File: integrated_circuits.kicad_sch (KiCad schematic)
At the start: 14 parts

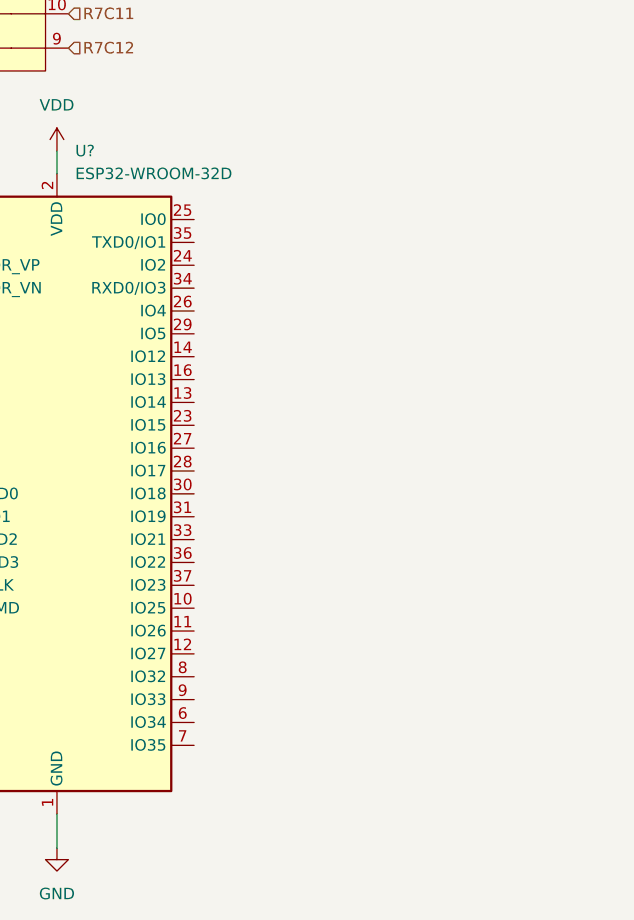
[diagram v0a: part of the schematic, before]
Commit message: Add MCU connections.
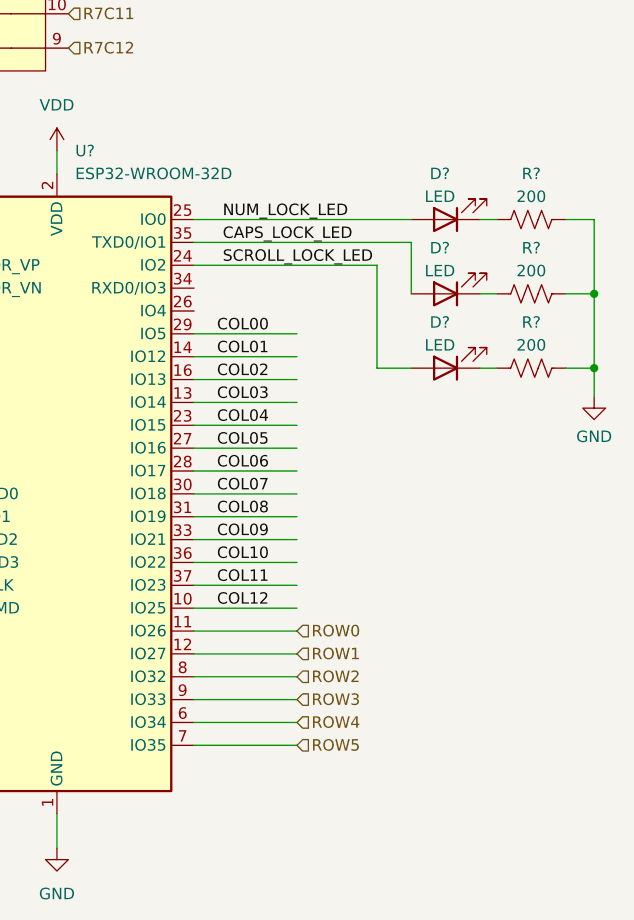
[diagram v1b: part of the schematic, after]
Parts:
- added D? (x3): LED, symbol Device:LED
- added R? (x3): 200, symbol Device:R_US
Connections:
- net GND: now also R?.2, R?.2, R?.2
- net COL12: now reaches U?.10 (IO25)
- net ROW0: now reaches U?.11 (IO26)
- net ROW1: now reaches U?.12 (IO27)
- net COL03: now reaches U?.13 (IO14)
- net COL01: now reaches U?.14 (IO12)
- net COL02: now reaches U?.16 (IO13)
- net COL04: now reaches U?.23 (IO15)
- net SCROLL_LOCK_LED: now reaches U?.24 (IO2)
- net SCROLL_LOCK_LED: now also D?.2 (A)
- net NUM_LOCK_LED: now reaches U?.25 (IO0)
- net NUM_LOCK_LED: now also D?.2 (A)
- net COL05: now reaches U?.27 (IO16)
- net COL06: now reaches U?.28 (IO17)
- net COL00: now reaches U?.29 (IO5)
- net COL07: now reaches U?.30 (IO18)
- net COL08: now reaches U?.31 (IO19)
- net COL09: now reaches U?.33 (IO21)
- net CAPS_LOCK_LED: now reaches U?.35 (TXD0/IO1)
- net CAPS_LOCK_LED: now also D?.2 (A)
- net COL10: now reaches U?.36 (IO22)
- net COL11: now reaches U?.37 (IO23)
- net ROW4: now reaches U?.6 (IO34)
- net ROW5: now reaches U?.7 (IO35)
- net ROW2: now reaches U?.8 (IO32)
- net ROW3: now reaches U?.9 (IO33)
- new net: D?.1 (K), R?.1 (x3)

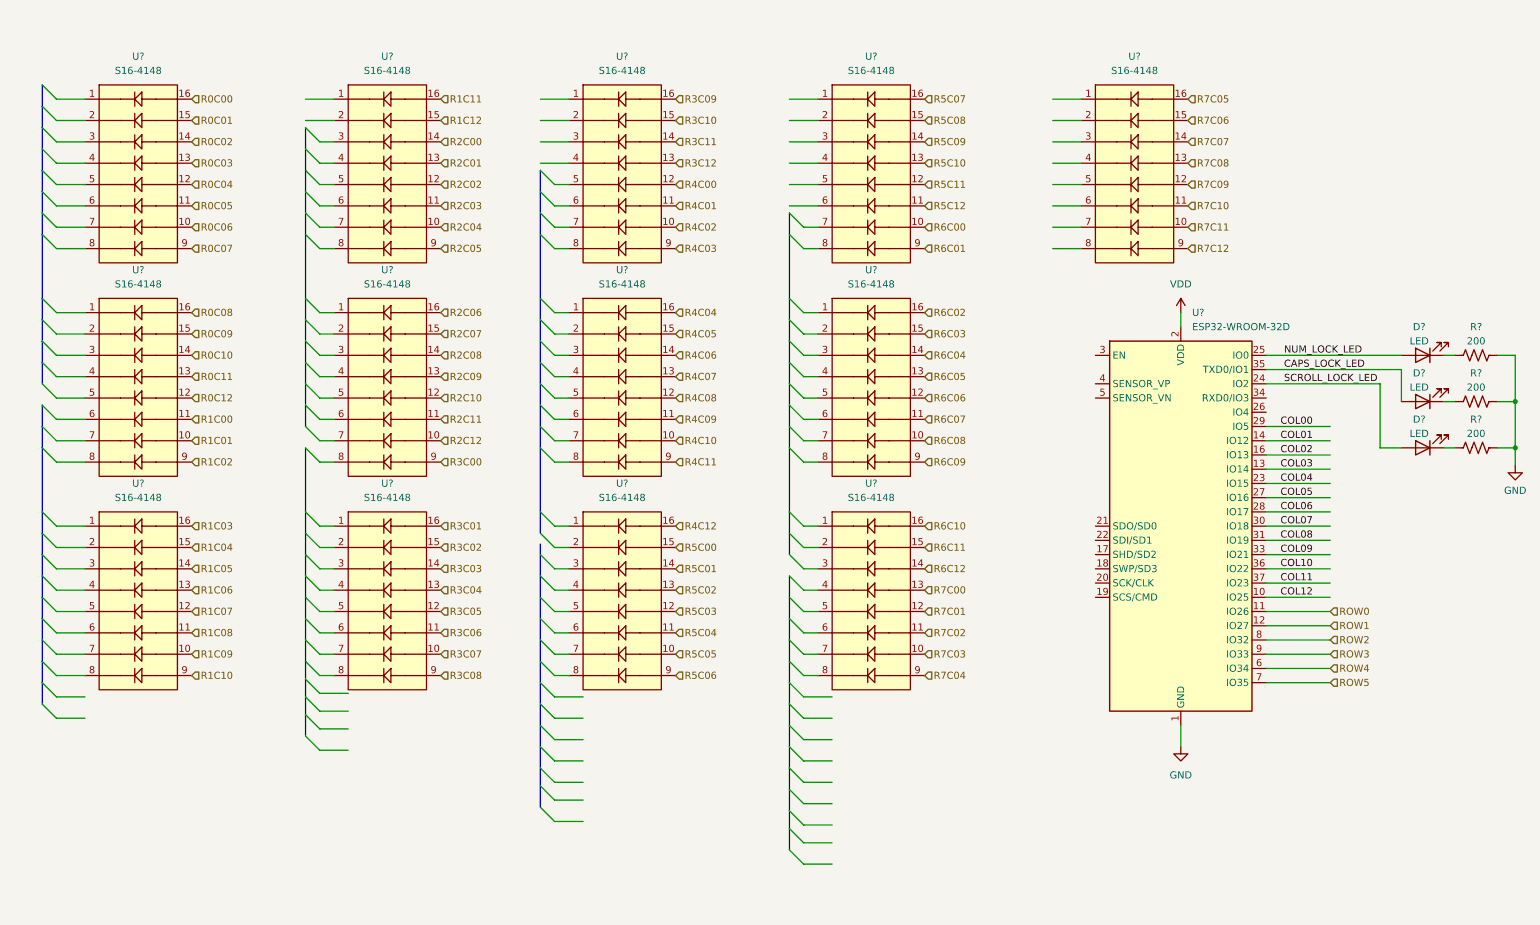
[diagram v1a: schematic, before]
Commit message: Add all connections to diode arrays.
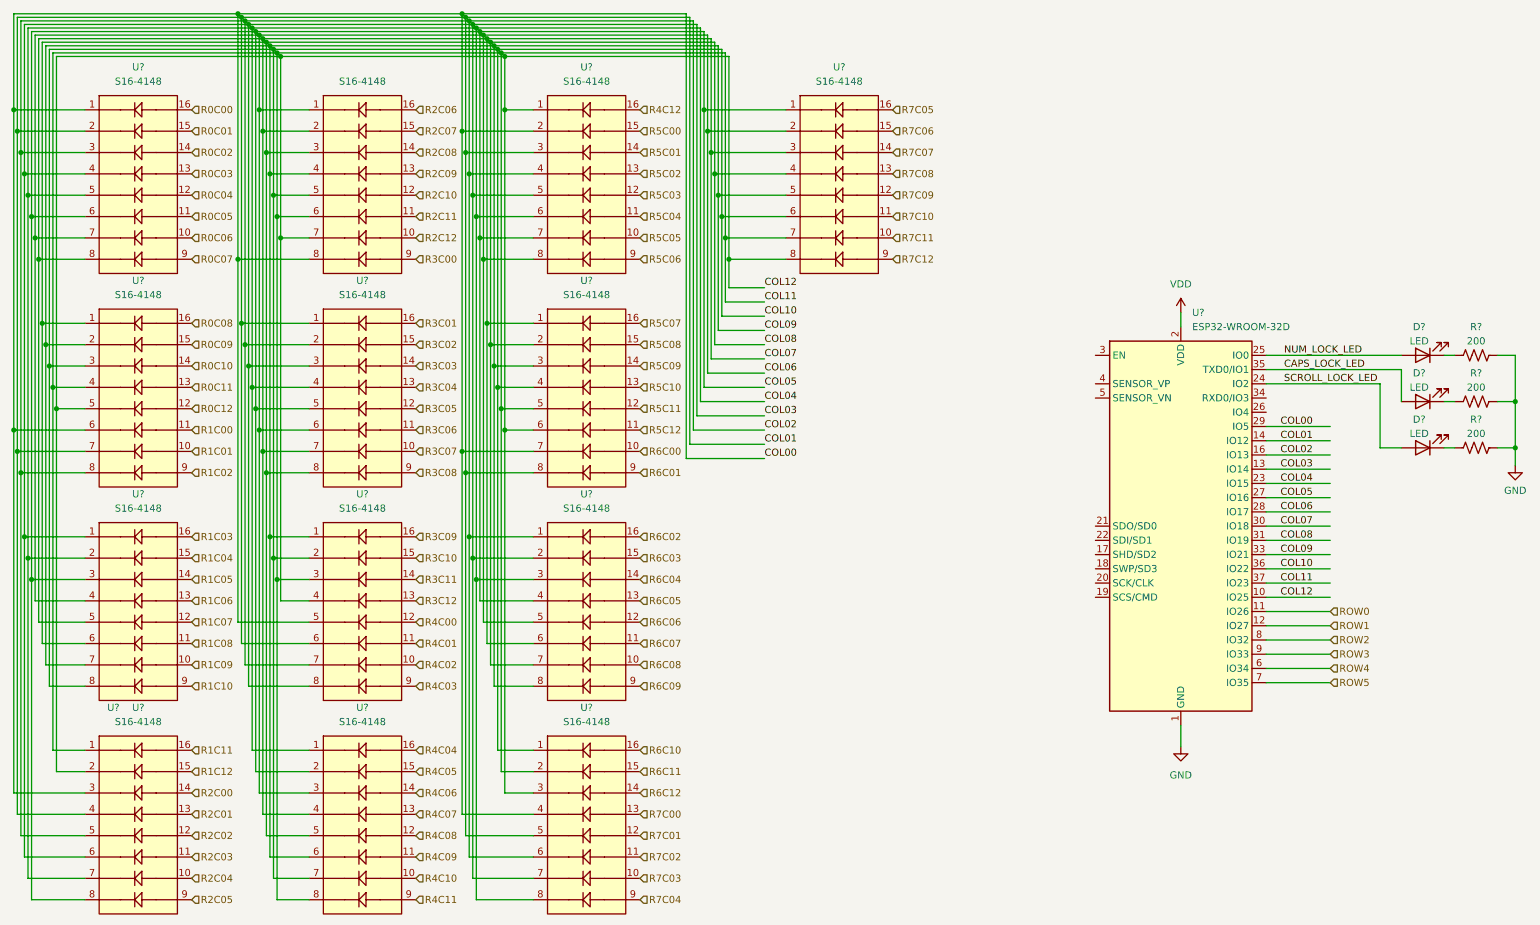
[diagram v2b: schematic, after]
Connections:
- net COL00: now also U?.1, U?.2, U?.3, U?.4, U?.5, U?.6, U?.7, U?.8
- net COL01: now also U?.1, U?.2, U?.3, U?.4, U?.5, U?.6, U?.7, U?.8
- net COL02: now also U?.1, U?.2, U?.3, U?.4, U?.5, U?.6, U?.7, U?.8
- net COL03: now also U?.1, U?.2, U?.3, U?.4, U?.5, U?.6, U?.7, U?.8
- net COL04: now also U?.1, U?.2, U?.3, U?.4, U?.5, U?.6, U?.7, U?.8
- net COL05: now also U?.1, U?.2, U?.3, U?.4, U?.5, U?.6, U?.7, U?.8
- net COL06: now also U?.1, U?.2, U?.3, U?.4, U?.5, U?.6, U?.7, U?.8
- net COL07: now also U?.1, U?.2, U?.3, U?.4, U?.5, U?.6, U?.7, U?.8
- net COL08: now also U?.1, U?.2, U?.3, U?.4, U?.5, U?.6, U?.7, U?.8
- net COL09: now also U?.1, U?.2, U?.3, U?.4, U?.5, U?.6, U?.7, U?.8
- net COL10: now also U?.1, U?.2, U?.3, U?.4, U?.5, U?.6, U?.7, U?.8
- net COL11: now also U?.1, U?.2, U?.3, U?.4, U?.5, U?.6, U?.7, U?.8
- net COL12: now also U?.1, U?.2, U?.3, U?.4, U?.5, U?.6, U?.7, U?.8
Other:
- moved on the sheet: U?

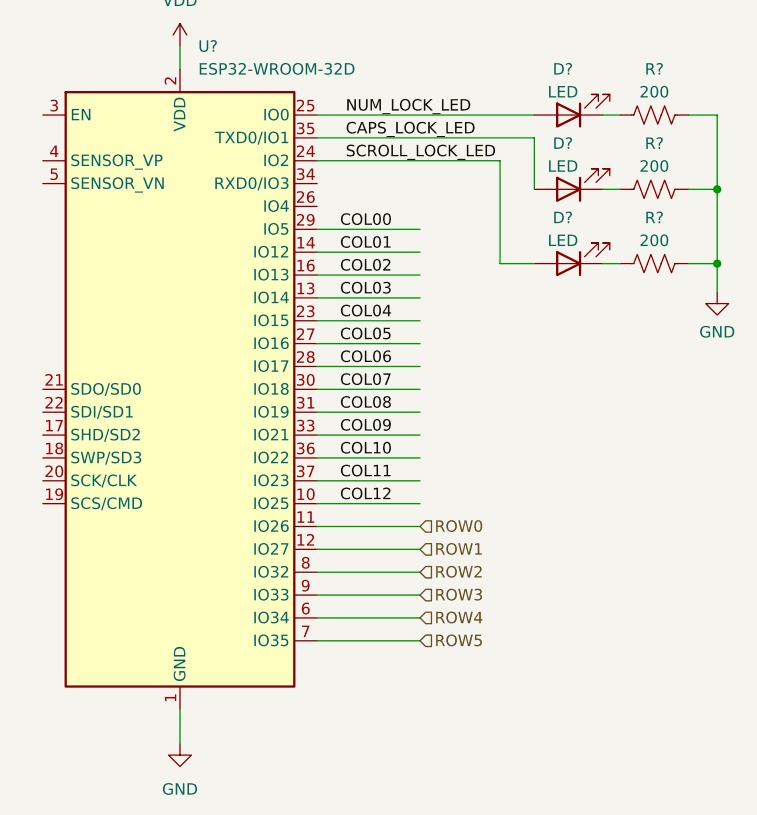
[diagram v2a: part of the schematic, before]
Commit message: Add MCU connections. Out of GPIO.
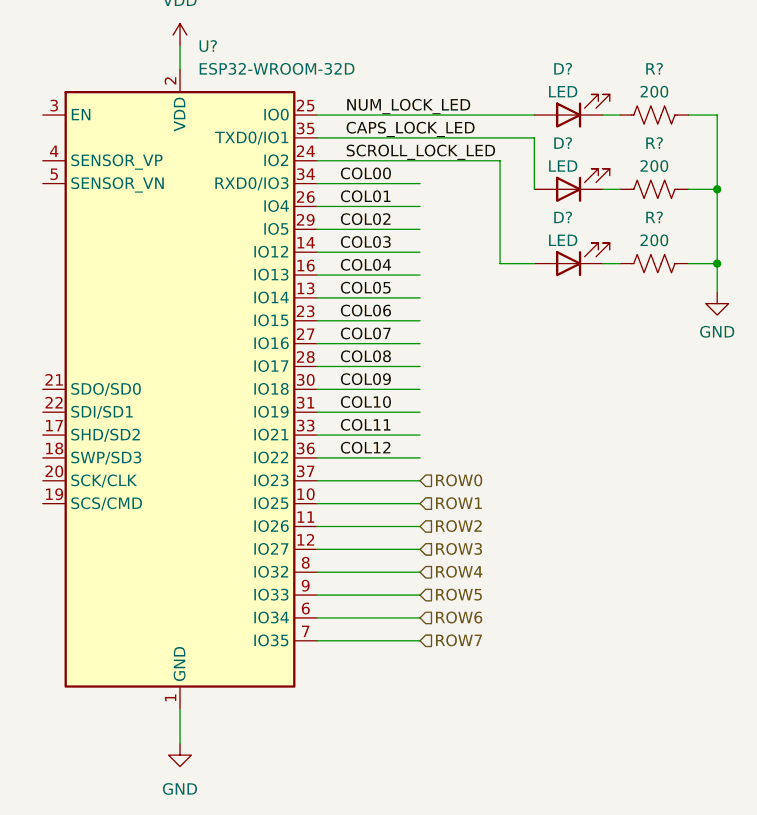
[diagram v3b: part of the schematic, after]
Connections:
- net COL00: now also U?.34 (RXD0/IO3); no longer U?.29 (IO5)
- net COL01: now also U?.26 (IO4); no longer U?.14 (IO12)
- net COL02: now also U?.29 (IO5); no longer U?.16 (IO13)
- net COL03: now also U?.14 (IO12); no longer U?.13 (IO14)
- net COL04: now also U?.16 (IO13); no longer U?.23 (IO15)
- net COL05: now also U?.13 (IO14); no longer U?.27 (IO16)
- net COL06: now also U?.23 (IO15); no longer U?.28 (IO17)
- net COL07: now also U?.27 (IO16); no longer U?.30 (IO18)
- net COL08: now also U?.28 (IO17); no longer U?.31 (IO19)
- net COL09: now also U?.30 (IO18); no longer U?.33 (IO21)
- net COL10: now also U?.31 (IO19); no longer U?.36 (IO22)
- net COL11: now also U?.33 (IO21); no longer U?.37 (IO23)
- net COL12: now also U?.36 (IO22); no longer U?.10 (IO25)
- net ROW0: now also U?.37 (IO23); no longer U?.11 (IO26)
- net ROW1: now also U?.10 (IO25); no longer U?.12 (IO27)
- net ROW2: now also U?.11 (IO26); no longer U?.8 (IO32)
- net ROW3: now also U?.12 (IO27); no longer U?.9 (IO33)
- net ROW4: now also U?.8 (IO32); no longer U?.6 (IO34)
- net ROW5: now also U?.9 (IO33); no longer U?.7 (IO35)
- new net ROW6: U?.6 (IO34)
- new net ROW7: U?.7 (IO35)
